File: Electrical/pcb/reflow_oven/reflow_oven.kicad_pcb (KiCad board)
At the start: 2 copper layers, 64 parts, among them J1 1711738, J2 Conn_01x06, J3 DB9_Female, P1 USB_C_Receptacle_USB2.0, U1 LH05-10B05, U2 AP1117-33, U3 STM32F030CCTx, U4 CP2102N-Axx-xQFN28, U5 MAX485E, Y1 8MHz 8pF

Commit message: analog Sensing
-voltage and current sensor
-zero crossing
-temperature
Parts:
- added C16: 100nF, Capacitor_SMD:C_0603_1608Metric, F.Cu at (-445.0, 17.1)
- added C17: 100nF, Capacitor_SMD:C_0603_1608Metric, F.Cu at (-455.5, 17.1)
- added C18: 100nF, Capacitor_SMD:C_0603_1608Metric, F.Cu at (-545.7, 19.2)
- added C19: 100nF, Capacitor_SMD:C_0603_1608Metric, F.Cu at (-501.3, -20.3)
- added C20: 100nF, Capacitor_SMD:C_0603_1608Metric, F.Cu at (-531.9, 4.24)
- added C21: 100nF, Capacitor_SMD:C_0603_1608Metric, F.Cu at (-515.3, -6.81)
- added C22: 100nF, Capacitor_SMD:C_0603_1608Metric, F.Cu at (-551.6, 25.1)
- added C23: 1uF, Capacitor_SMD:C_0805_2012Metric, F.Cu at (-509.5, -17.0)
- added C24: 1uF, Capacitor_SMD:C_0805_2012Metric, F.Cu at (-542.9, 13.3)
- added C25: 100nF, Capacitor_SMD:C_0603_1608Metric, F.Cu at (-526.2, 0.43)
- added C26: 1n, Capacitor_SMD:C_0603_1608Metric, F.Cu at (-519.3, -6.53)
- added C27: 1n, Capacitor_SMD:C_0603_1608Metric, F.Cu at (-496.0, -28.3)
- added C28: 4.7uF, Capacitor_SMD:C_0805_2012Metric, F.Cu at (-537.7, 8.89)
- added C29: 1uF, Capacitor_SMD:C_0805_2012Metric, F.Cu at (-515.6, -9.57)
- added C30: 1uF, Capacitor_SMD:C_0805_2012Metric, F.Cu at (-545.5, 16.5)
- added C31: 4.7uF, Capacitor_SMD:C_0805_2012Metric, F.Cu at (-513.9, -17.0)
- added C32: 1n, Capacitor_SMD:C_0603_1608Metric, F.Cu at (-500.9, -22.8)
- added C33: 1n, Capacitor_SMD:C_0603_1608Metric, F.Cu at (-534.0, 11.8)
- added C34: 100nF, Capacitor_SMD:C_0603_1608Metric, F.Cu at (-541.3, 18.6)
- added C35: 100nF, Capacitor_SMD:C_0603_1608Metric, F.Cu at (-505.3, -15.8)
- added C36: 100nF, Capacitor_SMD:C_0603_1608Metric, F.Cu at (-496.0, -25.8)
- added C37: 100nF, Capacitor_SMD:C_0603_1608Metric, F.Cu at (-522.2, 0.43)
- added D10: BAT54S, Package_TO_SOT_SMD:SOT-23, F.Cu at (-523.8, -5.56)
- added D11: BAT54S, Package_TO_SOT_SMD:SOT-23, F.Cu at (-530.7, 0.76)
- added D12: BAT54S, Package_TO_SOT_SMD:SOT-23, F.Cu at (-550.4, 21.6)
- added D13: BAT54S, Package_TO_SOT_SMD:SOT-23, F.Cu at (-505.2, -27.3)
- added D8: D_Bridge_+-AA, footprint_lib:DIP825W58P510L832H472Q4N, F.Cu at (-474.3, 23.4)
- added D9: D_TVS 5V, Diode_SMD:D_SOD-523, F.Cu at (-446.1, 32.6)
- added F5: Fuse, footprint_lib:Circular_fuse, F.Cu at (-473.3, 4.95)
- added F6: 250mA, footprint_lib:Circular_fuse, F.Cu at (-518.7, -24.4)
- added F7: 250mA, footprint_lib:Circular_fuse, F.Cu at (-564.7, 13.5)
- added J10: NTC_A IN, TerminalBlock_Phoenix:TerminalBlock_Phoenix_MPT-0,5-2-2.54_1x02_P2.54mm_Horizontal, F.Cu at (-544.1, 3.26)
- added J11: NTC_B IN, TerminalBlock_Phoenix:TerminalBlock_Phoenix_MPT-0,5-2-2.54_1x02_P2.54mm_Horizontal, F.Cu at (-531.3, -5.59)
- added J4: Line IN, TerminalBlock:TerminalBlock_bornier-2_P5.08mm, F.Cu at (-555.0, -5.19)
- added J5: Heater_A, TerminalBlock:TerminalBlock_bornier-2_P5.08mm, F.Cu at (-555.0, 3.86)
- added J6: Line IN, TerminalBlock:TerminalBlock_bornier-2_P5.08mm, F.Cu at (-566.5, 3.86)
- added J7: Heater_B, TerminalBlock:TerminalBlock_bornier-2_P5.08mm, F.Cu at (-566.5, -5.19)
- added J8: THC IN, TerminalBlock_Phoenix:TerminalBlock_Phoenix_MPT-0,5-2-2.54_1x02_P2.54mm_Horizontal, F.Cu at (-521.2, -15.2)
- added J9: THC IN, TerminalBlock_Phoenix:TerminalBlock_Phoenix_MPT-0,5-2-2.54_1x02_P2.54mm_Horizontal, F.Cu at (-538.9, -5.59)
- added JP1: boot, Jumper:SolderJumper-2_P1.3mm_Open_RoundedPad1.0x1.5mm, F.Cu at (-470.8, 34.6)
- added N1: Net-Tie_2, NetTie:NetTie-2_SMD_Pad2.0mm, F.Cu at (-586.6, 31.4)
- added R24: 22, Resistor_SMD:R_0603_1608Metric, F.Cu at (-440.3, 14.2)
- added R25: 22, Resistor_SMD:R_0603_1608Metric, F.Cu at (-441.0, 17.1)
- added R26: 120, Resistor_SMD:R_0805_2012Metric_Pad1.20x1.40mm_HandSolder, F.Cu at (-444.6, 14.4)
- added R27: 80K6, Resistor_SMD:R_0805_2012Metric_Pad1.20x1.40mm_HandSolder, F.Cu at (-461.3, 24.6)
- added R28: 80K6, Resistor_SMD:R_0805_2012Metric_Pad1.20x1.40mm_HandSolder, F.Cu at (-466.1, 24.6)
- added R29: 40K2, Resistor_SMD:R_1206_3216Metric_Pad1.30x1.75mm_HandSolder, F.Cu at (-466.1, 27.6)
- added R30: 40K2, Resistor_SMD:R_1206_3216Metric_Pad1.30x1.75mm_HandSolder, F.Cu at (-455.2, 14.4)
- added R31: 80K6, Resistor_SMD:R_0805_2012Metric_Pad1.20x1.40mm_HandSolder, F.Cu at (-560.7, 24.4)
- added R32: 40K2, Resistor_SMD:R_1206_3216Metric_Pad1.30x1.75mm_HandSolder, F.Cu at (-536.1, 0.18)
- added R33: 40K2, Resistor_SMD:R_1206_3216Metric_Pad1.30x1.75mm_HandSolder, F.Cu at (-548.1, 13.3)
- added R34: 80K6, Resistor_SMD:R_0805_2012Metric_Pad1.20x1.40mm_HandSolder, F.Cu at (-500.4, -28.0)
- added R35: 40K2, Resistor_SMD:R_1206_3216Metric_Pad1.30x1.75mm_HandSolder, F.Cu at (-510.6, -27.9)
- added R36: 40K2, Resistor_SMD:R_1206_3216Metric_Pad1.30x1.75mm_HandSolder, F.Cu at (-520.8, -9.43)
- added R37: 10K, Resistor_SMD:R_0603_1608Metric, F.Cu at (-529.5, 9.26)
- added R38: 10K, Resistor_SMD:R_0603_1608Metric, F.Cu at (-514.2, -14.2)
- added R39: 40K2, Resistor_SMD:R_1206_3216Metric_Pad1.30x1.75mm_HandSolder, F.Cu at (-510.6, -24.6)
- added R40: 40K2, Resistor_SMD:R_1206_3216Metric_Pad1.30x1.75mm_HandSolder, F.Cu at (-548.1, 10.0)
- added R41: 0, Resistor_SMD:R_0603_1608Metric, F.Cu at (-546.0, 24.2)
- added R42: 0, Resistor_SMD:R_0603_1608Metric, F.Cu at (-531.9, 6.75)
- added R43: 50, Resistor_SMD:R_0805_2012Metric_Pad1.20x1.40mm_HandSolder, F.Cu at (-505.2, -23.6)
- added R44: 50, Resistor_SMD:R_0805_2012Metric_Pad1.20x1.40mm_HandSolder, F.Cu at (-555.9, 24.4)
- added R45: 10K, Resistor_SMD:R_0603_1608Metric, F.Cu at (-510.2, -14.2)
- added R46: 10K, Resistor_SMD:R_0603_1608Metric, F.Cu at (-505.3, -18.4)
- added R47: 10K, Resistor_SMD:R_0603_1608Metric, F.Cu at (-546.0, 21.7)
- added R48: 10K, Resistor_SMD:R_0603_1608Metric, F.Cu at (-506.4, -20.9)
- added R49: 4K7, Resistor_SMD:R_0603_1608Metric, F.Cu at (-541.3, 16.1)
- added R50: 10K, Resistor_SMD:R_0603_1608Metric, F.Cu at (-580.4, 25.1)
- added R51: 10K, Resistor_SMD:R_0603_1608Metric, F.Cu at (-500.7, -25.3)
- added R52: 100K, Resistor_SMD:R_0603_1608Metric, F.Cu at (-527.9, 6.75)
- added R53: 100K, Resistor_SMD:R_0603_1608Metric, F.Cu at (-588.4, 25.1)
- added R54: 4K7, Resistor_SMD:R_0603_1608Metric, F.Cu at (-538.0, 11.6)
- added R55: 10K, Resistor_SMD:R_0603_1608Metric, F.Cu at (-533.5, 9.26)
- added R56: 10K, Resistor_SMD:R_0603_1608Metric, F.Cu at (-576.4, 25.1)
- added R57: 10K, Resistor_SMD:R_0603_1608Metric, F.Cu at (-524.2, -2.08)
- added R58: 10K, Resistor_SMD:R_0603_1608Metric, F.Cu at (-527.9, 4.24)
- added R59: 10K, Resistor_SMD:R_0603_1608Metric, F.Cu at (-511.4, -11.7)
- added R60: 10K, Resistor_SMD:R_0603_1608Metric, F.Cu at (-519.3, -4.02)
- added R61: 100K, Resistor_SMD:R_0603_1608Metric, F.Cu at (-572.4, 25.1)
- added R62: 100K, Resistor_SMD:R_0603_1608Metric, F.Cu at (-584.4, 25.1)
- added RV3: 10K, footprint_lib:TC33X2503E, F.Cu at (-556.2, 18.8)
- added RV4: 10K, footprint_lib:TC33X2503E, F.Cu at (-566.4, 22.4)
- added SW1: SW_MEC_5E, footprint_lib:KMR621NGLFS, F.Cu at (-456.8, 33.9)
- added T1: ZMPT101B, footprint_lib:ZMPT101B, F.Cu at (-562.9, -26.0)
- added T2: ZMPT101B, footprint_lib:ZMPT101B, F.Cu at (-539.9, -26.0)
- added U10: TLP2361, footprint_lib:11-4L1S_5-PIN-SOIC_, F.Cu at (-543.9, -5.47)
- added U11: COS6001, Package_TO_SOT_SMD:SOT-23-5, F.Cu at (-592.6, 10.2)
- added U12: COS6001, Package_TO_SOT_SMD:SOT-23-5, F.Cu at (-511.0, -20.7)
- added U13: COS6001, Package_TO_SOT_SMD:SOT-23-5, F.Cu at (-536.5, 4.05)
- added U14: COS6001, Package_TO_SOT_SMD:SOT-23-5, F.Cu at (-542.5, 9.61)
- added U6: MAX6675ISA+T, footprint_lib:SOIC127P600X175-8N, F.Cu at (-443.5, 3.56)
- added U7: MAX6675ISA+T, footprint_lib:SOIC127P600X175-8N, F.Cu at (-555.3, 11.7)
- added U8: ACS758LCB-050B-PFF, Sensor_Current:Allegro_CB_PFF, F.Cu at (-582.0, -4.34)
- added U9: ACS758LCB-050B-PFF, Sensor_Current:Allegro_CB_PFF, F.Cu at (-582.0, 22.4)
- C13: value 4.7uF -> 100nF; footprint Capacitor_SMD:C_0805_2012Metric -> Capacitor_SMD:C_0603_1608Metric
- C14: value 100nF -> 4.7uF; footprint Capacitor_SMD:C_0603_1608Metric -> Capacitor_SMD:C_0805_2012Metric
- J3: value DB9_Female -> DB9_Female_MountingHoles
- R10, R11: value 5.1k -> 22
- R12: value 22.1k -> 22
- R13: value 47.5k -> 5.1k
- R14: value 1k -> 5.1k
- R15: value 0 -> 22.1k
- R16: value 0 -> 47.5k
- R17: value 10K -> 1k
- R18: value 10K -> 0
- R19: value 22 -> 0
- R20, R21, R5, R9: value 22 -> 10K
- R23: value 120 -> 22; footprint Resistor_SMD:R_0805_2012Metric_Pad1.20x1.40mm_HandSolder -> Resistor_SMD:R_0603_1608Metric
- moved J3 73.0 mm to (-451.6, 48.9)
- moved C1 39.4 mm to (-369.0, 37.2)
- moved C12 39.4 mm to (-410.4, 45.0)
- moved C13 39.4 mm to (-418.8, 61.0)
- moved C15 39.4 mm to (-405.2, 6.88)
- moved C2 39.4 mm to (-367.8, 59.1)
- moved C4 39.4 mm to (-402.8, 34.1)
- moved D5 39.4 mm to (-406.8, 63.0)
- moved D6 39.4 mm to (-400.5, 53.3)
- moved D7 39.4 mm to (-384.3, -11.7)
- moved J1 39.4 mm to (-309.9, 21.0)
- moved P1 39.4 mm to (-415.3, 53.6)
- moved R13 39.4 mm to (-409.2, 6.88)
- moved R14 39.4 mm to (-398.5, 3.59)
- moved R17 39.4 mm to (-401.1, 6.54)
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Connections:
- net Net-(F1-Pad1) renamed VAC
- C13 pad 1: +3V3 -> /MCU_User/NRESET
- C5 pad 2: GNDA -> GND
- J3 pad 0: (no net) -> GND
- R10 pad 1: GND -> /MCU_User/ZeroCrossing
- R10 pad 2: Net-(P1-PadA5) -> Net-(U3-Pad2)
- R11 pad 1: GND -> /MCU_User/I2C1_SCL
- R11 pad 2: Net-(P1-PadB5) -> Net-(U3-Pad42)
- R12 pad 1: VBUS -> /MCU_User/I2C1_SDA
- R12 pad 2: Net-(R12-Pad2) -> Net-(U3-Pad43)
- R13 pad 2: Net-(R12-Pad2) -> Net-(P1-PadA5)
- R14 pad 1: Net-(R14-Pad1) -> GND
- R14 pad 2: +3V3 -> Net-(P1-PadB5)
- R15 pad 1: Net-(R15-Pad1) -> VBUS
- R15 pad 2: /Interfaces/RX_MCU_usb -> Net-(R15-Pad2)
- R16 pad 1: Net-(R16-Pad1) -> GND
- R16 pad 2: /Interfaces/TX_MCU_usb -> Net-(R15-Pad2)
- R17 pad 1: /Interfaces/~{RE}_485 -> Net-(R17-Pad1)
- R18 pad 1: GND -> Net-(R18-Pad1)
- R18 pad 2: /Interfaces/DE_485 -> /Interfaces/RX_MCU_usb
- R19 pad 1: /Interfaces/RX_MCU_485 -> Net-(R19-Pad1)
- R19 pad 2: Net-(R19-Pad2) -> /Interfaces/TX_MCU_usb
- R20 pad 2: Net-(R20-Pad2) -> +3V3
- R21 pad 1: /Interfaces/DE_485 -> GND
- R21 pad 2: Net-(R21-Pad2) -> /Interfaces/DE_485
- R22 pad 1: /Interfaces/TX_MCU_485 -> /Interfaces/RX_MCU_485
- R23 pad 1: Net-(F4-Pad1) -> /Interfaces/~{RE}_485
- R23 pad 2: Net-(F3-Pad1) -> Net-(R23-Pad2)
- R5 pad 1: Net-(J2-Pad5) -> /MCU_User/BOOT
- R5 pad 2: /MCU_User/SWCLK -> GND
- R6 pad 1: Net-(J2-Pad4) -> Net-(J2-Pad5)
- R6 pad 2: /MCU_User/SWDIO -> /MCU_User/SWCLK
- R7 pad 1: Net-(J2-Pad3) -> Net-(J2-Pad4)
- R7 pad 2: /MCU_User/NRESET -> /MCU_User/SWDIO
- R8 pad 1: /MCU_User/I2C1_SCL -> Net-(J2-Pad3)
- R8 pad 2: Net-(U3-Pad42) -> /MCU_User/NRESET
- R9 pad 1: /MCU_User/I2C1_SDA -> VDD
- R9 pad 2: Net-(U3-Pad43) -> /MCU_User/NRESET
- U3 pad 10: unconnected-(U3-Pad10) -> /Interfaces/~{RE}_485
- U3 pad 11: unconnected-(U3-Pad11) -> /Interfaces/DE_485
- U3 pad 12: /MCU_User/TX_MCU_485 -> /Interfaces/TX_MCU_485
- U3 pad 14: unconnected-(U3-Pad14) -> /MCU_User/~{CS}_A
- U3 pad 15: unconnected-(U3-Pad15) -> /MCU_User/SPI_CLK
- U3 pad 16: unconnected-(U3-Pad16) -> /MCU_User/SPI_MISO
- U3 pad 2: /MCU_User/SWDIO -> Net-(U3-Pad2)
- U3 pad 29: unconnected-(U3-Pad29) -> /MCU_User/~{CS}_B
- U3 pad 3: /MCU_User/SWCLK -> unconnected-(U3-Pad3)
- U3 pad 34: unconnected-(U3-Pad34) -> /MCU_User/SWDIO
- U3 pad 37: unconnected-(U3-Pad37) -> /MCU_User/SWCLK
- U3 pad 44: unconnected-(U3-Pad44) -> /MCU_User/BOOT
- U4 pad 25: Net-(R16-Pad1) -> Net-(R19-Pad1)
- U4 pad 26: Net-(R15-Pad1) -> Net-(R18-Pad1)
- U4 pad 8: Net-(R12-Pad2) -> Net-(R15-Pad2)
- U4 pad 9: Net-(R14-Pad1) -> Net-(R17-Pad1)
- U5 pad 1: Net-(R19-Pad2) -> Net-(R22-Pad2)
- U5 pad 2: Net-(R20-Pad2) -> Net-(R23-Pad2)
- U5 pad 3: Net-(R21-Pad2) -> Net-(R24-Pad2)
- U5 pad 4: Net-(R22-Pad2) -> Net-(R25-Pad2)

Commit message: Update reflow_oven.kicad_pcb
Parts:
- moved C23 30.0 mm to (-502.9, 12.2)
- moved C32 30.0 mm to (-494.2, 6.41)
- moved U12 30.0 mm to (-504.4, 8.50)
- moved C19 30.0 mm to (-494.6, 8.92)
- moved C27 30.0 mm to (-489.3, 0.95)
- moved C35 30.0 mm to (-498.6, 13.4)
- moved D13 30.0 mm to (-498.5, 1.92)
- moved N1 30.0 mm to (-580.0, 60.6)
- moved R34 30.0 mm to (-493.7, 1.17)
- moved R35 30.0 mm to (-504.0, 1.34)
- moved R39 30.0 mm to (-504.0, 4.63)
- moved R43 30.0 mm to (-498.6, 5.62)
- moved R45 30.0 mm to (-503.5, 15.0)
- moved R46 30.0 mm to (-498.6, 10.9)
- moved R48 30.0 mm to (-499.8, 8.35)
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
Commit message: schematic
-interface
-micro
todo
output
routing
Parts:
- added J12: NTC_A IN, TerminalBlock_Phoenix:TerminalBlock_Phoenix_MPT-0,5-2-2.54_1x02_P2.54mm_Horizontal, F.Cu at (-516.3, 58.2)
- added J13: NTC_B IN, TerminalBlock_Phoenix:TerminalBlock_Phoenix_MPT-0,5-2-2.54_1x02_P2.54mm_Horizontal, F.Cu at (-523.9, 58.2)
- added R63: 10K, Resistor_SMD:R_0603_1608Metric, F.Cu at (-509.2, 55.3)
- added R64: 10K, Resistor_SMD:R_0603_1608Metric, F.Cu at (-516.4, 63.6)
- added R65: 100K, Resistor_SMD:R_0603_1608Metric, F.Cu at (-520.4, 63.6)
- added R66: 100K, Resistor_SMD:R_0603_1608Metric, F.Cu at (-524.4, 63.6)
- J10: value NTC_A IN -> THC IN
- J11: value NTC_B IN -> THC IN
- J3: value DB9_Female_MountingHoles -> USER BOARD DISPLAY; footprint Connector_Dsub:DSUB-9_Female_Horizontal_P2.77x2.84mm_EdgePinOffset7.70mm_Housed_MountingHolesOffset9.12mm -> footprint_lib:SHDR10W66P254_2X5_2019X914X986P
- J4: value Line IN -> USER BOARD BUTTON; footprint TerminalBlock:TerminalBlock_bornier-2_P5.08mm -> footprint_lib:SHDR10W66P254_2X5_2019X914X986P
- J5: value Heater_A -> DB9_Female_MountingHoles; footprint TerminalBlock:TerminalBlock_bornier-2_P5.08mm -> Connector_Dsub:DSUB-9_Female_Horizontal_P2.77x2.84mm_EdgePinOffset7.70mm_Housed_MountingHolesOffset9.12mm
- J7: value Heater_B -> Heater_A
- J8: value THC IN -> Line IN; footprint TerminalBlock_Phoenix:TerminalBlock_Phoenix_MPT-0,5-2-2.54_1x02_P2.54mm_Horizontal -> TerminalBlock:TerminalBlock_bornier-2_P5.08mm
- J9: value THC IN -> Heater_B; footprint TerminalBlock_Phoenix:TerminalBlock_Phoenix_MPT-0,5-2-2.54_1x02_P2.54mm_Horizontal -> TerminalBlock:TerminalBlock_bornier-2_P5.08mm
- R13, R14: value 5.1k -> 22
- R15: value 22.1k -> 22
- R16: value 47.5k -> 22
- R17: value 1k -> 5.1k
- R18: value 0 -> 5.1k
- R19: value 0 -> 22.1k
- R20: value 10K -> 47.5k
- R21: value 10K -> 1k
- R22, R23: value 22 -> 0
- R24, R25: value 22 -> 10K
- R26: value 120 -> 22; footprint Resistor_SMD:R_0805_2012Metric_Pad1.20x1.40mm_HandSolder -> Resistor_SMD:R_0603_1608Metric
- R27, R28: value 80K6 -> 22; footprint Resistor_SMD:R_0805_2012Metric_Pad1.20x1.40mm_HandSolder -> Resistor_SMD:R_0603_1608Metric
- R29: value 40K2 -> 22; footprint Resistor_SMD:R_1206_3216Metric_Pad1.30x1.75mm_HandSolder -> Resistor_SMD:R_0603_1608Metric
- R30: value 40K2 -> 120; footprint Resistor_SMD:R_1206_3216Metric_Pad1.30x1.75mm_HandSolder -> Resistor_SMD:R_0805_2012Metric_Pad1.20x1.40mm_HandSolder
- R32, R35: value 40K2 -> 80K6; footprint Resistor_SMD:R_1206_3216Metric_Pad1.30x1.75mm_HandSolder -> Resistor_SMD:R_0805_2012Metric_Pad1.20x1.40mm_HandSolder
- R34: value 80K6 -> 40K2; footprint Resistor_SMD:R_0805_2012Metric_Pad1.20x1.40mm_HandSolder -> Resistor_SMD:R_1206_3216Metric_Pad1.30x1.75mm_HandSolder
- R37: value 10K -> 40K2; footprint Resistor_SMD:R_0603_1608Metric -> Resistor_SMD:R_1206_3216Metric_Pad1.30x1.75mm_HandSolder
- R38: value 10K -> 80K6; footprint Resistor_SMD:R_0603_1608Metric -> Resistor_SMD:R_0805_2012Metric_Pad1.20x1.40mm_HandSolder
- R41, R42: value 0 -> 10K
- R43, R44: value 50 -> 40K2; footprint Resistor_SMD:R_0805_2012Metric_Pad1.20x1.40mm_HandSolder -> Resistor_SMD:R_1206_3216Metric_Pad1.30x1.75mm_HandSolder
- R45, R46: value 10K -> 0
- R47, R48: value 10K -> 50; footprint Resistor_SMD:R_0603_1608Metric -> Resistor_SMD:R_0805_2012Metric_Pad1.20x1.40mm_HandSolder
- R49, R54: value 4K7 -> 10K
- R52, R61, R62: value 100K -> 10K
- R53: value 100K -> 4K7
- R56, R57: value 10K -> 100K
- R58: value 10K -> 4K7
- moved J8 94.2 mm to (-618.6, -24.8)
- moved J9 72.8 mm to (-618.7, 19.5)
- moved J4 70.7 mm to (-497.4, 40.9)
- moved J7 49.7 mm to (-618.5, -8.84)
- moved J6 47.6 mm to (-618.9, 6.45)
- moved J5 36.6 mm to (-545.4, 54.4)
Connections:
- J10 pad 1: GNDA -> Net-(U6-Pad3)
- J10 pad 2: /Sensors/NTC_A -> GNDA
- J11 pad 1: GNDA -> Net-(J11-Pad1)
- J11 pad 2: /Sensors/NTC_B -> GNDA
- J3 pad 1: unconnected-(J3-Pad1) -> +3V3
- J3 pad 2: unconnected-(J3-Pad2) -> +3V3
- J3 pad 3: /Interfaces/B -> /Interfaces/SPI2_CLK
- J3 pad 4: unconnected-(J3-Pad4) -> /Interfaces/SPI2_MOSI_RW
- J3 pad 5: GND -> /Interfaces/LCD_RST
- J3 pad 6: unconnected-(J3-Pad6) -> /Interfaces/LCD_CS
- J3 pad 7: /Interfaces/A -> /MCU_User/I2C1_SCL
- J3 pad 8: unconnected-(J3-Pad8) -> /MCU_User/I2C1_SDA
- J3 pad 9: unconnected-(J3-Pad9) -> GND
- J4 pad 1: Net-(J4-Pad1) -> +3V3
- J4 pad 2: Net-(F6-Pad1) -> +3V3
- J5 pad 1: Net-(J5-Pad1) -> unconnected-(J5-Pad1)
- J5 pad 2: Net-(J4-Pad1) -> unconnected-(J5-Pad2)
- J6 pad 2: Net-(F7-Pad1) -> Net-(F6-Pad1)
- J8 pad 1: Net-(U6-Pad3) -> Net-(J8-Pad1)
- J8 pad 2: GNDA -> Net-(F7-Pad1)
- J9 pad 2: GNDA -> Net-(J8-Pad1)
- R13 pad 1: GND -> /MCU_User/LCD_CS
- R13 pad 2: Net-(P1-PadA5) -> Net-(U3-Pad25)
- R14 pad 1: GND -> /MCU_User/SPI2_CLK
- R14 pad 2: Net-(P1-PadB5) -> Net-(U3-Pad26)
- R15 pad 1: VBUS -> /MCU_User/LCD_RST
- R15 pad 2: Net-(R15-Pad2) -> Net-(U3-Pad27)
- R16 pad 1: GND -> /MCU_User/SPI2_MOSI_RW
- R16 pad 2: Net-(R15-Pad2) -> Net-(U3-Pad28)
- R17 pad 1: Net-(R17-Pad1) -> GND
- R17 pad 2: +3V3 -> Net-(P1-PadA5)
- R18 pad 1: Net-(R18-Pad1) -> GND
- R18 pad 2: /Interfaces/RX_MCU_usb -> Net-(P1-PadB5)
- R19 pad 1: Net-(R19-Pad1) -> VBUS
- R19 pad 2: /Interfaces/TX_MCU_usb -> Net-(R19-Pad2)
- R20 pad 1: /Interfaces/~{RE}_485 -> GND
- R20 pad 2: +3V3 -> Net-(R19-Pad2)
- R21 pad 1: GND -> Net-(R21-Pad1)
- R21 pad 2: /Interfaces/DE_485 -> +3V3
- R22 pad 1: /Interfaces/RX_MCU_485 -> Net-(R22-Pad1)
- R22 pad 2: Net-(R22-Pad2) -> /Interfaces/RX_MCU_usb
- R23 pad 1: /Interfaces/~{RE}_485 -> Net-(R23-Pad1)
- R23 pad 2: Net-(R23-Pad2) -> /Interfaces/TX_MCU_usb
- R24 pad 1: /Interfaces/DE_485 -> /Interfaces/~{RE}_485
- R24 pad 2: Net-(R24-Pad2) -> +3V3
- R25 pad 1: /Interfaces/TX_MCU_485 -> GND
- R25 pad 2: Net-(R25-Pad2) -> /Interfaces/DE_485
- R26 pad 1: Net-(F4-Pad1) -> /Interfaces/RX_MCU_485
- R26 pad 2: Net-(F3-Pad1) -> Net-(R26-Pad2)
- R27 pad 1: Net-(D8-Pad1) -> /Interfaces/~{RE}_485
- R28 pad 1: Net-(R27-Pad2) -> /Interfaces/DE_485
- R29 pad 1: Net-(F6-Pad2) -> /Interfaces/TX_MCU_485
- R30 pad 1: Net-(F7-Pad2) -> Net-(F4-Pad1)
- R30 pad 2: Net-(R30-Pad2) -> Net-(F3-Pad1)
- R31 pad 1: Net-(R28-Pad2) -> Net-(D8-Pad1)
- R32 pad 1: Net-(R29-Pad2) -> Net-(R31-Pad2)
- R33 pad 1: Net-(R30-Pad2) -> Net-(F6-Pad2)
- R34 pad 1: Net-(R31-Pad2) -> Net-(F7-Pad2)
- R34 pad 2: Net-(D9-Pad2) -> Net-(R34-Pad2)
- R37 pad 1: VDDA -> Net-(R34-Pad2)
- R37 pad 2: /MCU_User/~{CS}_A -> Net-(R37-Pad2)
- R38 pad 1: VDDA -> Net-(R35-Pad2)
- R38 pad 2: /MCU_User/~{CS}_B -> Net-(D9-Pad2)
- R39 pad 1: Net-(R39-Pad1) -> Net-(R36-Pad2)
- R39 pad 2: Net-(R35-Pad2) -> Net-(R39-Pad2)
- R40 pad 1: Net-(R40-Pad1) -> Net-(R37-Pad2)
- R40 pad 2: Net-(R36-Pad2) -> Net-(R40-Pad2)
- R41 pad 1: /Sensors/Csense_A -> VDDA
- R41 pad 2: Net-(R41-Pad2) -> /MCU_User/~{CS}_A
- R42 pad 1: /Sensors/Csense_B -> VDDA
- R42 pad 2: Net-(R42-Pad2) -> /MCU_User/~{CS}_B
- R43 pad 2: Net-(C23-Pad1) -> Net-(R39-Pad2)
- R44 pad 2: Net-(C24-Pad1) -> Net-(R40-Pad2)
- R45 pad 1: Net-(C26-Pad1) -> /Sensors/Csense_A
- R45 pad 2: Net-(C23-Pad2) -> Net-(R45-Pad2)
- R46 pad 1: Net-(R43-Pad1) -> /Sensors/Csense_B
- R46 pad 2: VDDA -> Net-(R46-Pad2)
- R47 pad 1: Net-(C27-Pad1) -> Net-(R47-Pad1)
- R47 pad 2: Net-(C24-Pad2) -> Net-(C23-Pad1)
- R48 pad 1: Net-(R44-Pad1) -> Net-(R48-Pad1)
- R48 pad 2: VDDA -> Net-(C24-Pad1)
- R49 pad 1: VDDA -> Net-(C26-Pad1)
- R49 pad 2: /Sensors/NTC_A -> Net-(C23-Pad2)
- R50 pad 1: Net-(R43-Pad1) -> Net-(R47-Pad1)
- R50 pad 2: GNDA -> VDDA
- R51 pad 1: Net-(R44-Pad1) -> Net-(C27-Pad1)
- R51 pad 2: GNDA -> Net-(C24-Pad2)
- R52 pad 1: Net-(C26-Pad2) -> Net-(R48-Pad1)
- R52 pad 2: Net-(C26-Pad1) -> VDDA
- R53 pad 1: Net-(C27-Pad2) -> VDDA
- R53 pad 2: Net-(C27-Pad1) -> /Sensors/NTC_A
- R54 pad 1: VDDA -> Net-(R47-Pad1)
- R54 pad 2: /Sensors/NTC_B -> GNDA
- R55 pad 1: Net-(C32-Pad1) -> Net-(R48-Pad1)
- R55 pad 2: Net-(C29-Pad2) -> GNDA
- R56 pad 1: Net-(R56-Pad1) -> Net-(C26-Pad2)
- R56 pad 2: VDDA -> Net-(C26-Pad1)
- R57 pad 1: Net-(C33-Pad1) -> Net-(C27-Pad2)
- R57 pad 2: Net-(C30-Pad2) -> Net-(C27-Pad1)
- R58 pad 1: Net-(R58-Pad1) -> VDDA
- R58 pad 2: VDDA -> /Sensors/NTC_B
- R59 pad 1: Net-(R56-Pad1) -> Net-(C32-Pad1)
- R59 pad 2: GNDA -> Net-(C29-Pad2)
- R60 pad 1: Net-(R58-Pad1) -> Net-(R60-Pad1)
- R60 pad 2: GNDA -> VDDA
- R61 pad 1: /Sensors/Vsense_A -> Net-(C33-Pad1)
- R61 pad 2: Net-(C32-Pad1) -> Net-(C30-Pad2)
- R62 pad 1: /Sensors/Vsense_B -> Net-(R62-Pad1)
- R62 pad 2: Net-(C33-Pad1) -> VDDA
- T1 pad 1: Net-(R39-Pad1) -> Net-(R43-Pad1)
- T1 pad 2: Net-(J4-Pad1) -> Net-(J6-Pad1)
- T1 pad 3: Net-(R43-Pad1) -> Net-(R47-Pad1)
- T2 pad 1: Net-(R40-Pad1) -> Net-(R44-Pad1)
- T2 pad 2: Net-(J6-Pad1) -> Net-(J8-Pad1)
- T2 pad 3: Net-(R44-Pad1) -> Net-(R48-Pad1)
- U11 pad 3: Net-(R43-Pad1) -> Net-(R47-Pad1)
- U12 pad 3: Net-(R44-Pad1) -> Net-(R48-Pad1)
- U13 pad 3: Net-(R56-Pad1) -> Net-(R60-Pad1)
- U14 pad 3: Net-(R58-Pad1) -> Net-(R62-Pad1)
- U3 pad 25: unconnected-(U3-Pad25) -> Net-(U3-Pad25)
- U3 pad 26: unconnected-(U3-Pad26) -> Net-(U3-Pad26)
- U3 pad 27: unconnected-(U3-Pad27) -> Net-(U3-Pad27)
- U3 pad 28: unconnected-(U3-Pad28) -> Net-(U3-Pad28)
- U4 pad 25: Net-(R19-Pad1) -> Net-(R23-Pad1)
- U4 pad 26: Net-(R18-Pad1) -> Net-(R22-Pad1)
- U4 pad 8: Net-(R15-Pad2) -> Net-(R19-Pad2)
- U4 pad 9: Net-(R17-Pad1) -> Net-(R21-Pad1)
- U5 pad 1: Net-(R22-Pad2) -> Net-(R26-Pad2)
- U5 pad 2: Net-(R23-Pad2) -> Net-(R27-Pad2)
- U5 pad 3: Net-(R24-Pad2) -> Net-(R28-Pad2)
- U5 pad 4: Net-(R25-Pad2) -> Net-(R29-Pad2)
- U7 pad 3: Net-(J9-Pad1) -> Net-(J11-Pad1)
- U8 pad 3: Net-(R41-Pad2) -> Net-(R45-Pad2)
- U8 pad 5: Net-(J5-Pad1) -> Net-(J7-Pad1)
- U9 pad 3: Net-(R42-Pad2) -> Net-(R46-Pad2)
- U9 pad 5: Net-(J7-Pad1) -> Net-(J9-Pad1)

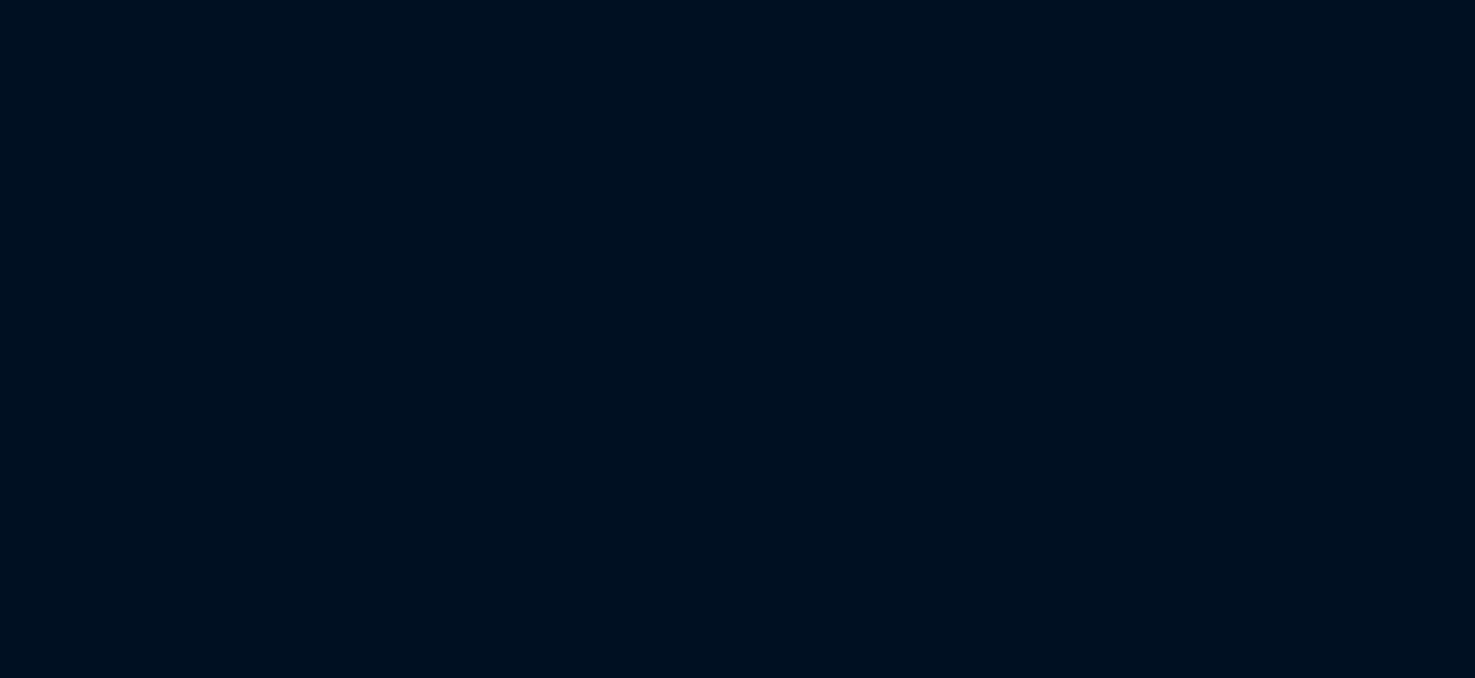
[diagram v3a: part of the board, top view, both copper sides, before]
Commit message: functionality
done output stage
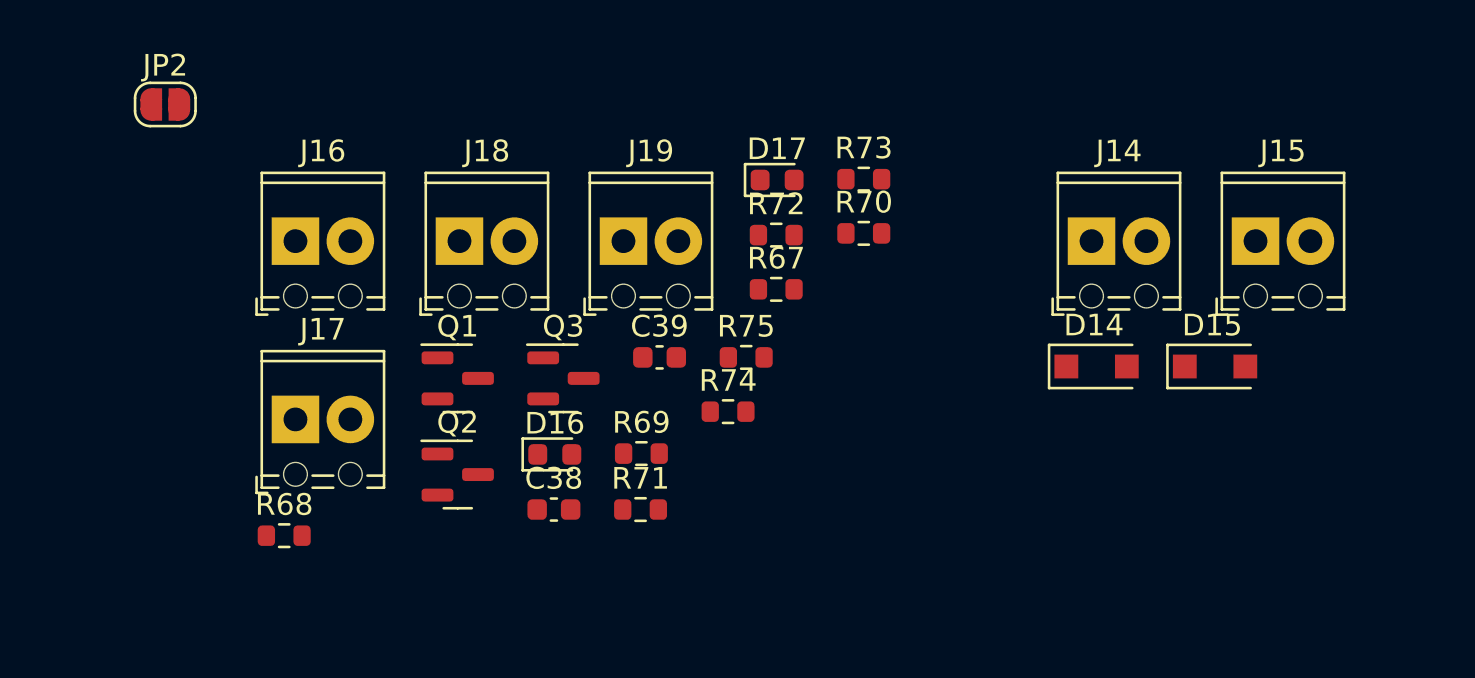
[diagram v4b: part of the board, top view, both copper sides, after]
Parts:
- added C38: 100nF, Capacitor_SMD:C_0603_1608Metric, F.Cu at (-499.9, -26.2)
- added C39: 100nF, Capacitor_SMD:C_0603_1608Metric, F.Cu at (-495.0, -33.2)
- added D14: DSS34, Diode_SMD:D_SOD-123F, F.Cu at (-474.8, -32.8)
- added D15: DSS34, Diode_SMD:D_SOD-123F, F.Cu at (-469.3, -32.8)
- added D16: LED, LED_SMD:LED_0603_1608Metric, F.Cu at (-499.8, -28.7)
- added D17: LED, LED_SMD:LED_0603_1608Metric, F.Cu at (-489.5, -41.4)
- added J14: 3V3 out, TerminalBlock_Phoenix:TerminalBlock_Phoenix_MPT-0,5-2-2.54_1x02_P2.54mm_Horizontal, F.Cu at (-475.0, -38.6)
- added J15: 5V out, TerminalBlock_Phoenix:TerminalBlock_Phoenix_MPT-0,5-2-2.54_1x02_P2.54mm_Horizontal, F.Cu at (-467.4, -38.6)
- added J16: SSR_A, TerminalBlock_Phoenix:TerminalBlock_Phoenix_MPT-0,5-2-2.54_1x02_P2.54mm_Horizontal, F.Cu at (-511.8, -38.6)
- added J17: FAN power in, TerminalBlock_Phoenix:TerminalBlock_Phoenix_MPT-0,5-2-2.54_1x02_P2.54mm_Horizontal, F.Cu at (-511.8, -30.3)
- added J18: FAN out, TerminalBlock_Phoenix:TerminalBlock_Phoenix_MPT-0,5-2-2.54_1x02_P2.54mm_Horizontal, F.Cu at (-504.2, -38.6)
- added J19: SSR_B, TerminalBlock_Phoenix:TerminalBlock_Phoenix_MPT-0,5-2-2.54_1x02_P2.54mm_Horizontal, F.Cu at (-496.7, -38.6)
- added JP2: SolderJumper_2_Open, Jumper:SolderJumper-2_P1.3mm_Open_RoundedPad1.0x1.5mm, F.Cu at (-517.9, -44.9)
- added Q1: DMN13H750S, Package_TO_SOT_SMD:SOT-23, F.Cu at (-504.3, -32.2)
- added Q2: AO3402, Package_TO_SOT_SMD:SOT-23, F.Cu at (-504.3, -27.8)
- added Q3: DMN13H750S, Package_TO_SOT_SMD:SOT-23, F.Cu at (-499.4, -32.2)
- added R67: 100, Resistor_SMD:R_0603_1608Metric, F.Cu at (-489.6, -36.4)
- added R68: 100k, Resistor_SMD:R_0603_1608Metric, F.Cu at (-512.4, -25.0)
- added R69: 100, Resistor_SMD:R_0603_1608Metric, F.Cu at (-495.8, -28.8)
- added R70: 100k, Resistor_SMD:R_0603_1608Metric, F.Cu at (-485.5, -38.9)
- added R71: 1k, Resistor_SMD:R_0603_1608Metric, F.Cu at (-495.9, -26.2)
- added R72: 10K, Resistor_SMD:R_0603_1608Metric, F.Cu at (-489.6, -38.9)
- added R73: 100, Resistor_SMD:R_0603_1608Metric, F.Cu at (-485.5, -41.5)
- added R74: 100k, Resistor_SMD:R_0603_1608Metric, F.Cu at (-491.8, -30.7)
- added R75: 1k, Resistor_SMD:R_0603_1608Metric, F.Cu at (-491.0, -33.2)
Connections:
- net Net-(C2-Pad1) renamed +5V
- C28 pad 1: /Sensors/NTC_A -> /MCU_User/NTC_A
- C31 pad 1: /Sensors/NTC_B -> /MCU_User/NTC_B
- J12 pad 2: /Sensors/NTC_A -> /MCU_User/NTC_A
- J13 pad 2: /Sensors/NTC_B -> /MCU_User/NTC_B
- R13 pad 1: /MCU_User/LCD_CS -> /Interfaces/LCD_CS
- R14 pad 1: /MCU_User/SPI2_CLK -> /Interfaces/SPI2_CLK
- R15 pad 1: /MCU_User/LCD_RST -> /Interfaces/LCD_RST
- R16 pad 1: /MCU_User/SPI2_MOSI_RW -> /Interfaces/SPI2_MOSI_RW
- R53 pad 2: /Sensors/NTC_A -> /MCU_User/NTC_A
- R58 pad 2: /Sensors/NTC_B -> /MCU_User/NTC_B
- U3 pad 10: /Interfaces/~{RE}_485 -> /Sensors/Vsense_A
- U3 pad 11: /Interfaces/DE_485 -> /Sensors/Vsense_B
- U3 pad 14: /MCU_User/~{CS}_A -> /Sensors/Csense_A
- U3 pad 16: /MCU_User/SPI_MISO -> /Sensors/Csense_B
- U3 pad 17: unconnected-(U3-Pad17) -> /MCU_User/SPI_MOSI
- U3 pad 18: unconnected-(U3-Pad18) -> /MCU_User/NTC_A
- U3 pad 19: unconnected-(U3-Pad19) -> /MCU_User/NTC_B
- U3 pad 20: unconnected-(U3-Pad20) -> /Interfaces/OK_BTN
- U3 pad 21: unconnected-(U3-Pad21) -> /Interfaces/RT_BTN
- U3 pad 22: unconnected-(U3-Pad22) -> /Interfaces/LT_BTN
- U3 pad 3: unconnected-(U3-Pad3) -> /Interfaces/~{RE}_485
- U3 pad 32: unconnected-(U3-Pad32) -> /MCU_User/~{CS}_A
- U3 pad 33: unconnected-(U3-Pad33) -> /Interfaces/UP_BTN
- U3 pad 38: unconnected-(U3-Pad38) -> /Actuation/SSR_B
- U3 pad 39: unconnected-(U3-Pad39) -> /Actuation/SSR_A
- U3 pad 4: unconnected-(U3-Pad4) -> /Interfaces/DE_485
- U3 pad 40: unconnected-(U3-Pad40) -> /MCU_User/SPI_MISO
- U3 pad 41: unconnected-(U3-Pad41) -> /Interfaces/BUZZER
- U3 pad 45: unconnected-(U3-Pad45) -> /Actuation/FAN
- U3 pad 46: unconnected-(U3-Pad46) -> /Interfaces/DWN_BTN

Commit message: pcb layout
initial pcb layout
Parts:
- moved R41 943.2 mm to (389.8, 39.6)
- moved R53 938.4 mm to (342.6, 40.9)
- moved T1 936.9 mm to (366.1, -37.4)
- moved J10 928.5 mm to (376.9, 33.0)
- moved U7 924.8 mm to (362.1, 33.9)
- moved C22 920.8 mm to (361.8, 40.4)
- moved T2 913.6 mm to (364.6, -63.5)
- moved C21 907.6 mm to (384.4, 39.2)
- moved J5 896.6 mm to (348.6, 123.7)
- moved C39 896.4 mm to (367.5, 210.9)
- moved R74 896.2 mm to (371.2, 211.0)
- moved Q3 895.4 mm to (362.1, 211.7)
- moved R42 895.1 mm to (355.7, 40.3)
- moved R68 894.9 mm to (352.0, 206.7)
- moved R75 893.6 mm to (369.9, 206.3)
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
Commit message: pcb layout
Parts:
- J7: value Heater_A -> Line IN
- moved C25 285.3 mm to (38.8, 213.8)
- moved F6 238.4 mm to (180.3, 115.6), turned to 90 degrees
- moved R62 207.5 mm to (219.0, -83.4)
- moved T1 206.7 mm to (159.7, -48.3)
- moved T2 206.2 mm to (162.1, -102.7)
- moved U11 203.4 mm to (208.9, -35.0)
- moved C17 198.3 mm to (204.2, 134.6), turned to 90 degrees
- moved R61 191.8 mm to (215.0, -83.4)
- moved D12 180.8 mm to (229.1, -30.7)
- moved R50 179.7 mm to (198.8, -38.9)
- moved R56 179.7 mm to (202.8, -38.9)
- moved RV3 178.8 mm to (221.0, -31.2)
- moved C19 177.0 mm to (208.3, 131.3), turned to 180 degrees
- moved RV4 176.0 mm to (205.3, -83.8)
- moved U8 175.9 mm to (201.1, 135.2), turned to 90 degrees
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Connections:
- J6 pad 1: Net-(J6-Pad1) -> Net-(F6-Pad1)
- J6 pad 2: Net-(F6-Pad1) -> Net-(J6-Pad2)
- J7 pad 1: Net-(J7-Pad1) -> Net-(J6-Pad2)
- J7 pad 2: Net-(J6-Pad1) -> Net-(U8-Pad5)
- T1 pad 2: Net-(J6-Pad1) -> Net-(J6-Pad2)
- U8 pad 5: Net-(J7-Pad1) -> Net-(U8-Pad5)
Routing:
- net Net-(J6-Pad2): track 0.00 -> 10.1 mm
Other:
- board text added: "AC_L"
- board text added: "AC_N"
